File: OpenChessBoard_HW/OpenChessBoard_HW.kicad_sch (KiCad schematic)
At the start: 0 parts

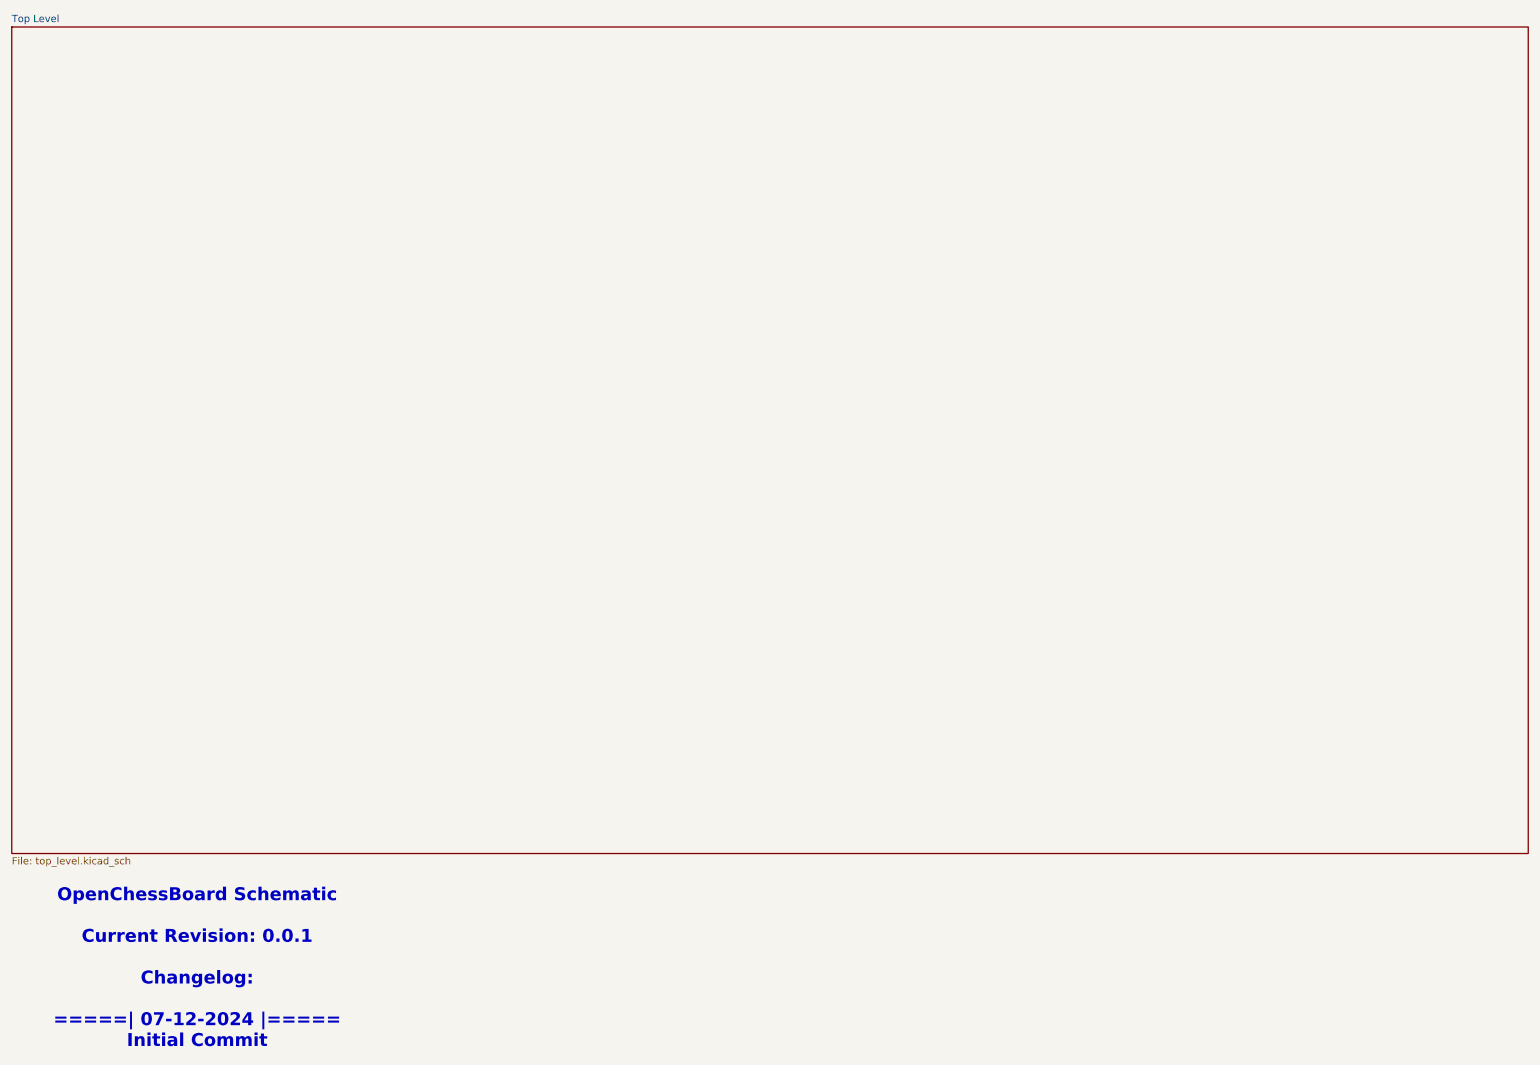
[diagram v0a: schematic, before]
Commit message: Added Basic Tile layout and Main Board
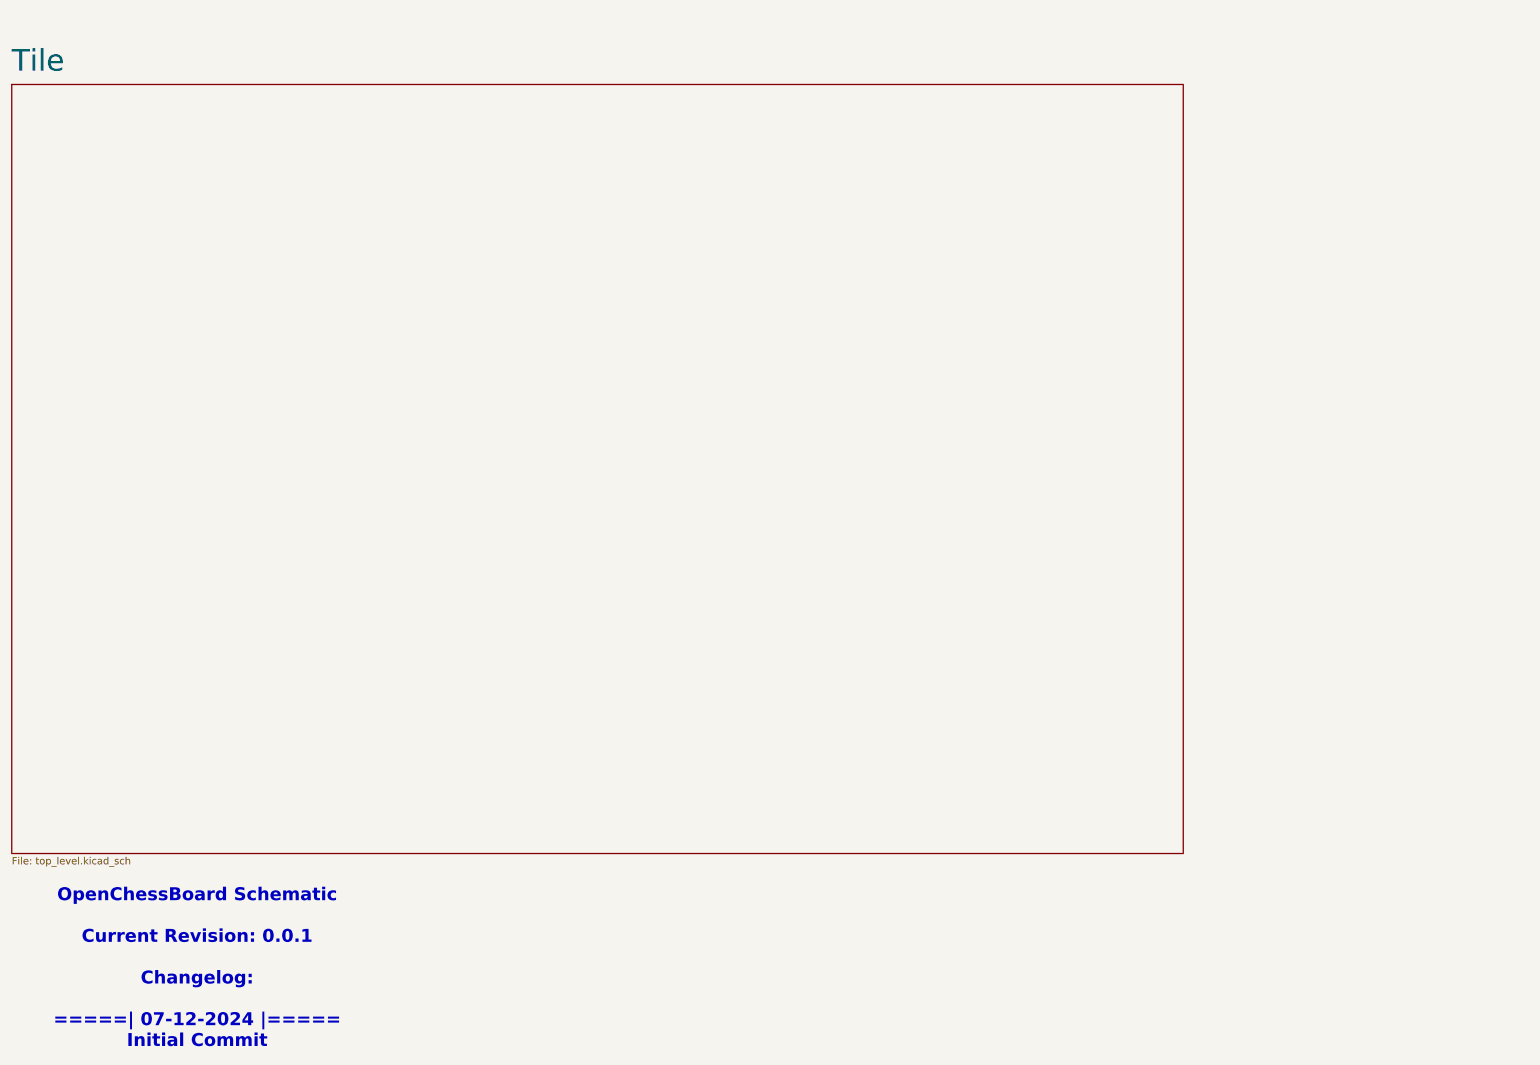
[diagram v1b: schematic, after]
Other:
- sheet Top Level renamed Tile
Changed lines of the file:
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@@
 	)
 	(sheet
-		(at 13.97 13.97)
-		(size 267.97 146.05)
+		(at 13.97 24.13)
+		(size 207.01 135.89)
 		(fields_autoplaced yes)
 		(stroke
@@
 			(color 0 0 0 0.0000)
 		)
-		(property "Sheetname" "Top Level"
-			(at 13.97 13.2584 0)
+		(property "Sheetname" "Tile"
+			(at 13.97 22.1484 0)
 			(effects
 				(font
-					(size 1.27 1.27)
+					(size 3.81 3.81)
 				)
 				(justify left bottom)
